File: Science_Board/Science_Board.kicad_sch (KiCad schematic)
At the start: 55 parts, among them J1 Conn_01x02, J10 Conn_01x02, J11 Conn_01x03, J12 Conn_01x03, J13 Conn_01x03, J14 Conn_01x03, J15 Conn_01x03, J16 Conn_01x03, J17 Conn_01x03, J18 Conn_01x03, J19 Conn_01x02, J2 RJ45_LED_Shielded, J20 Molex_Megafit_02, J22 Molex_Megafit_02, J23 Conn_01x02, J5 Conn_01x02, J6 Conn_01x04, J7 Conn_01x03, J8 Conn_01x03, J9 Conn_01x02, Q5 NMOS, SW1 SW_Push, SW10 SW_Push, SW11 SW_Push, SW12 SW_SPDT, SW2 SW_Push, SW3 SW_Push, SW4 SW_Push, SW5 SW_Push, SW6 SW_Push, SW7 SW_Push, SW8 SW_Push, SW9 SW_Push, U5 PCA9685BS

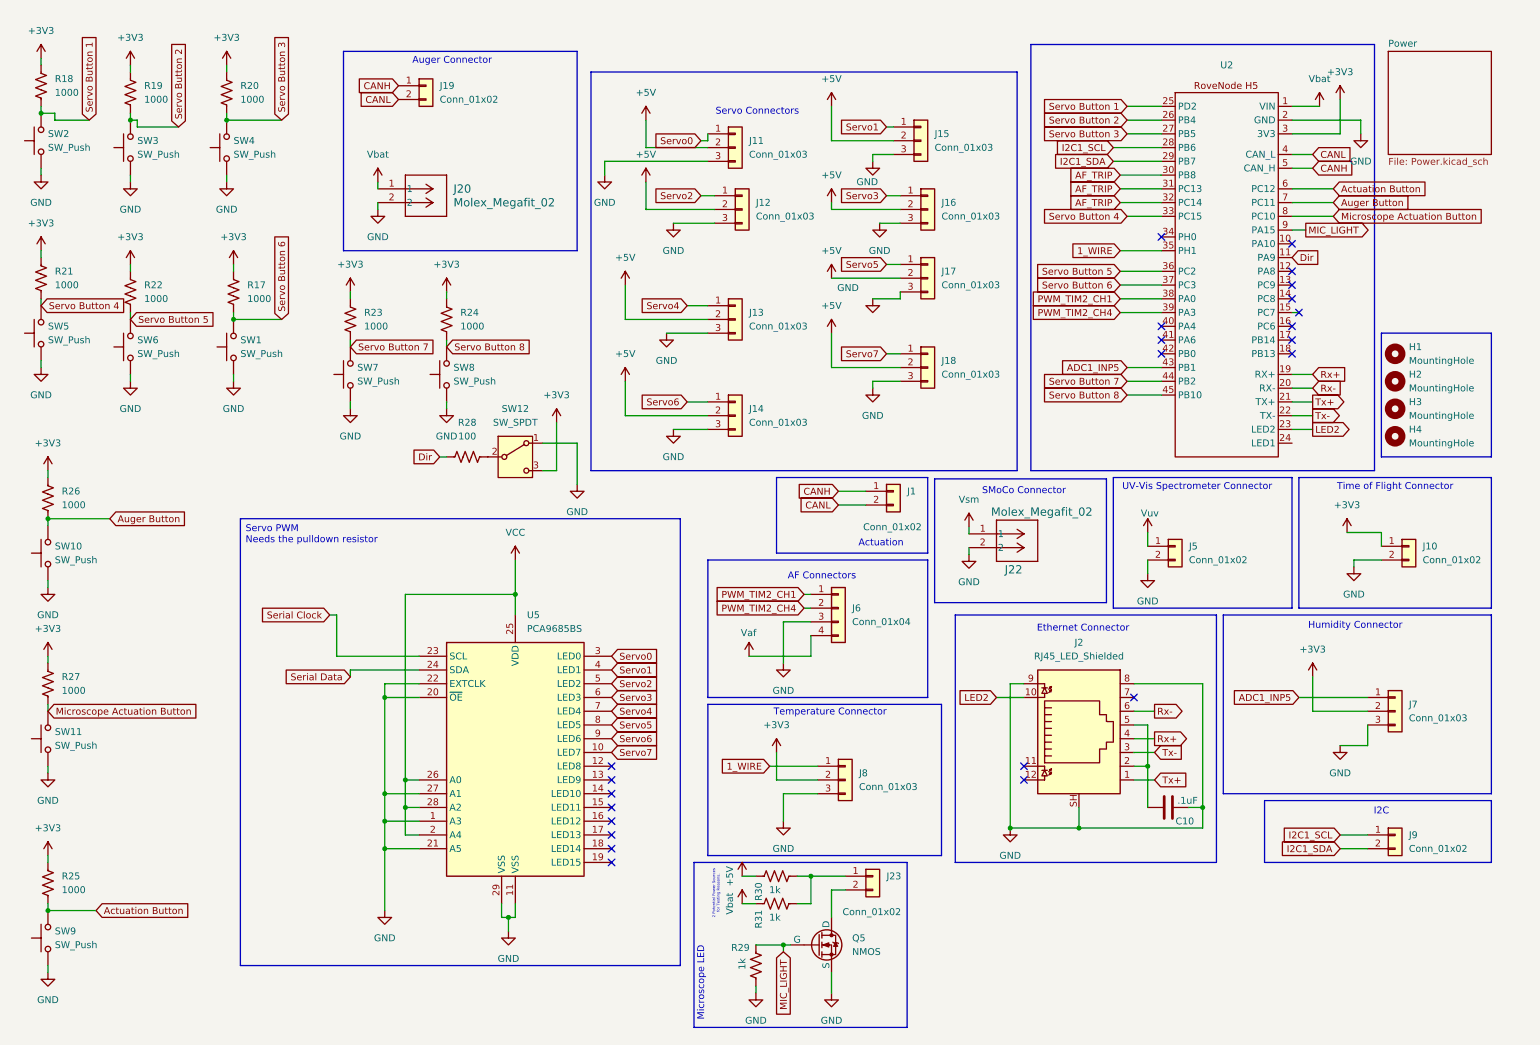
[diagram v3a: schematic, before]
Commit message: Incorrect Efuse Package, fixed and added gpio connections for loadswitch functionality
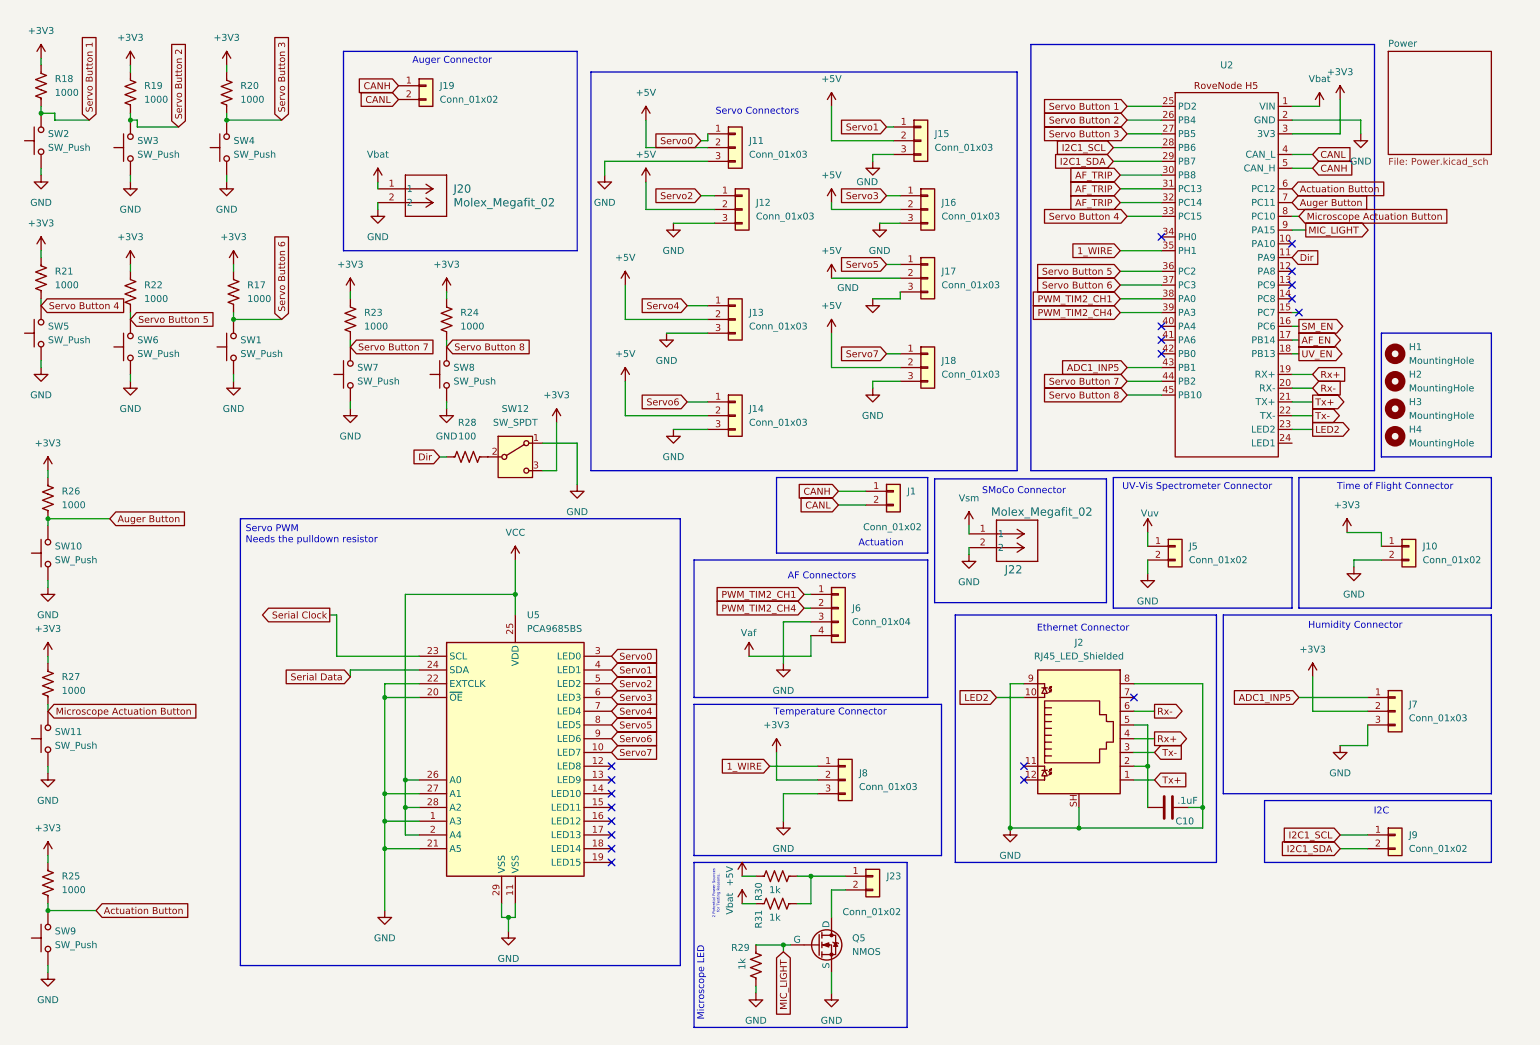
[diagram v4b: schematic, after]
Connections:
- net SM_EN: now reaches U2.16 (PC6)
- net AF_EN: now reaches U2.17 (PB14)
- net UV_EN: now reaches U2.18 (PB13)
- no-connect marks 23 -> 20
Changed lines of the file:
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@@
 	(paper "A4")
 	(rectangle
-		(start 138.43 135.89)
+		(start 135.89 135.89)
 		(end 181.61 163.83)
 		(stroke
@@
 	)
 	(rectangle
-		(start 138.43 109.22)
+		(start 135.89 109.22)
 		(end 179.07 134.62)
 		(stroke
@@
 	)
 	(no_connect
-		(at 246.38 71.12)
-	)
-	(no_connect
 		(at 120.65 162.56)
 	)
 	(no_connect
-		(at 246.38 66.04)
-	)
-	(no_connect
 		(at 246.38 55.88)
 	)
@@
 	)
 	(no_connect
-		(at 246.38 68.58)
-	)
-	(no_connect
 		(at 196.85 149.86)
 	)
@@
 	(wire
 		(pts
+			(xy 246.38 68.58) (xy 247.65 68.58)
+		)
+		(stroke
+			(width 0)
+			(type default)
+		)
+	)
+	(wire
+		(pts
 			(xy 152.4 180.34) (xy 153.67 180.34)
 		)
@@
 	(wire
 		(pts
-			(xy 246.38 43.18) (xy 254 43.18)
-		)
-		(stroke
-			(width 0)
-			(type default)
-		)
-	)
-	(wire
-		(pts
 			(xy 215.9 27.94) (xy 222.25 27.94)
 		)
@@
 	(wire
 		(pts
-			(xy 186.69 104.394) (xy 186.69 103.124)
-		)
-		(stroke
-			(width 0)
-			(type default)
-		)
-	)
-	(wire
-		(pts
 			(xy 171.45 29.21) (xy 172.72 29.21)
 		)
@@
 	(wire
 		(pts
+			(xy 186.69 102.87) (xy 186.69 104.394)
+		)
+		(stroke
+			(width 0)
+			(type default)
+		)
+	)
+	(wire
+		(pts
 			(xy 102.87 172.72) (xy 102.87 175.26)
 		)
@@
 	(wire
 		(pts
-			(xy 246.38 45.72) (xy 254 45.72)
+			(xy 246.38 45.72) (xy 247.65 45.72)
 		)
 		(stroke
@@
 	(wire
 		(pts
+			(xy 246.38 71.12) (xy 247.65 71.12)
+		)
+		(stroke
+			(width 0)
+			(type default)
+		)
+	)
+	(wire
+		(pts
 			(xy 215.9 45.72) (xy 222.25 45.72)
 		)
@@
 	(wire
 		(pts
-			(xy 246.38 40.64) (xy 254 40.64)
-		)
-		(stroke
-			(width 0)
-			(type default)
-		)
-	)
-	(wire
-		(pts
 			(xy 255.27 143.51) (xy 260.35 143.51)
 		)
@@
 	(wire
 		(pts
+			(xy 246.38 66.04) (xy 247.65 66.04)
+		)
+		(stroke
+			(width 0)
+			(type default)
+		)
+	)
+	(wire
+		(pts
 			(xy 171.45 71.12) (xy 173.99 71.12)
 		)
@@
 	)
 	(global_label "Serial Clock"
-		(shape input)
+		(shape output)
 		(at 68.58 119.38 180)
 		(fields_autoplaced yes)
@@
 	(global_label "Microscope Actuation Button"
 		(shape input)
-		(at 254 45.72 0)
+		(at 247.65 45.72 0)
 		(fields_autoplaced yes)
 		(effects
@@
 		)
 		(property "Intersheetrefs" "${INTERSHEET_REFS}"
-			(at 284.5015 45.72 0)
+			(at 278.1515 45.72 0)
 			(hide yes)
 			(show_name no)
@@
 		)
 	)
+	(global_label "UV_EN"
+		(shape output)
+		(at 247.65 71.12 0)
+		(fields_autoplaced yes)
+		(effects
+			(font
+				(size 1.27 1.27)
+				(thickness 0.1588)
+			)
+			(justify left)
+		)
+		(property "Intersheetrefs" "${INTERSHEET_REFS}"
+			(at 256.5014 71.12 0)
+			(hide yes)
+			(show_name no)
+			(do_not_autoplace no)
+			(effects
+				(font
+					(size 1.27 1.27)
+				)
+				(justify left)
+			)
+		)
+	)
 	(global_label "ADC1_INP5"
 		(shape input)
@@
 	(global_label "Actuation Button"
 		(shape input)
-		(at 254 40.64 0)
+		(at 246.38 40.64 0)
 		(fields_autoplaced yes)
 		(effects
@@
 		)
 		(property "Intersheetrefs" "${INTERSHEET_REFS}"
-			(at 272.9506 40.64 0)
+			(at 265.3306 40.64 0)
 			(hide yes)
 			(show_name no)
@@
 		)
 	)
+	(global_label "SM_EN"
+		(shape output)
+		(at 247.65 66.04 0)
+		(fields_autoplaced yes)
+		(effects
+			(font
+				(size 1.27 1.27)
+				(thickness 0.1588)
+			)
+			(justify left)
+		)
+		(property "Intersheetrefs" "${INTERSHEET_REFS}"
+			(at 256.7432 66.04 0)
+			(hide yes)
+			(show_name no)
+			(do_not_autoplace no)
+			(effects
+				(font
+					(size 1.27 1.27)
+				)
+				(justify left)
+			)
+		)
+	)
 	(global_label "MIC_LIGHT"
 		(shape output)
@@
 		)
 	)
+	(global_label "AF_EN"
+		(shape output)
+		(at 247.65 68.58 0)
+		(fields_autoplaced yes)
+		(effects
+			(font
+				(size 1.27 1.27)
+				(thickness 0.1588)
+			)
+			(justify left)
+		)
+		(property "Intersheetrefs" "${INTERSHEET_REFS}"
+			(at 256.2595 68.58 0)
+			(hide yes)
+			(show_name no)
+			(do_not_autoplace no)
+			(effects
+				(font
+					(size 1.27 1.27)
+				)
+				(justify left)
+			)
+		)
+	)
 	(global_label "Servo Button 1"
 		(shape input)
@@
 	(global_label "Auger Button"
 		(shape input)
-		(at 254 43.18 0)
+		(at 246.38 43.18 0)
 		(fields_autoplaced yes)
 		(effects
@@
 		)
 		(property "Intersheetrefs" "${INTERSHEET_REFS}"
-			(at 269.3826 43.18 0)
+			(at 261.7626 43.18 0)
 			(hide yes)
 			(show_name no)
@@
 	(symbol
 		(lib_id "power:VCC")
-		(at 186.69 103.124 0)
+		(at 186.69 102.87 0)
 		(unit 1)
 		(body_style 1)
@@
 		(fields_autoplaced yes)
 		(property "Reference" "#PWR093"
-			(at 186.69 106.934 0)
+			(at 186.69 106.68 0)
 			(hide yes)
 			(show_name no)
@@
 		)
 		(property "Value" "Vsm"
-			(at 186.69 98.044 0)
+			(at 186.69 97.79 0)
 			(show_name no)
 			(do_not_autoplace no)
@@
 		)
 		(property "Footprint" "MRDT_Connectors:MOLEX_MegaFit_02_Horizontal"
-			(at 186.69 103.124 0)
+			(at 186.69 102.87 0)
 			(hide yes)
 			(show_name no)
@@
 		)
 		(property "Datasheet" ""
-			(at 186.69 103.124 0)
+			(at 186.69 102.87 0)
 			(hide yes)
 			(show_name no)
@@
 		)
 		(property "Description" "Power symbol creates a global label with name \"VCC\""
-			(at 186.69 103.124 0)
+			(at 186.69 102.87 0)
 			(hide yes)
 			(show_name no)

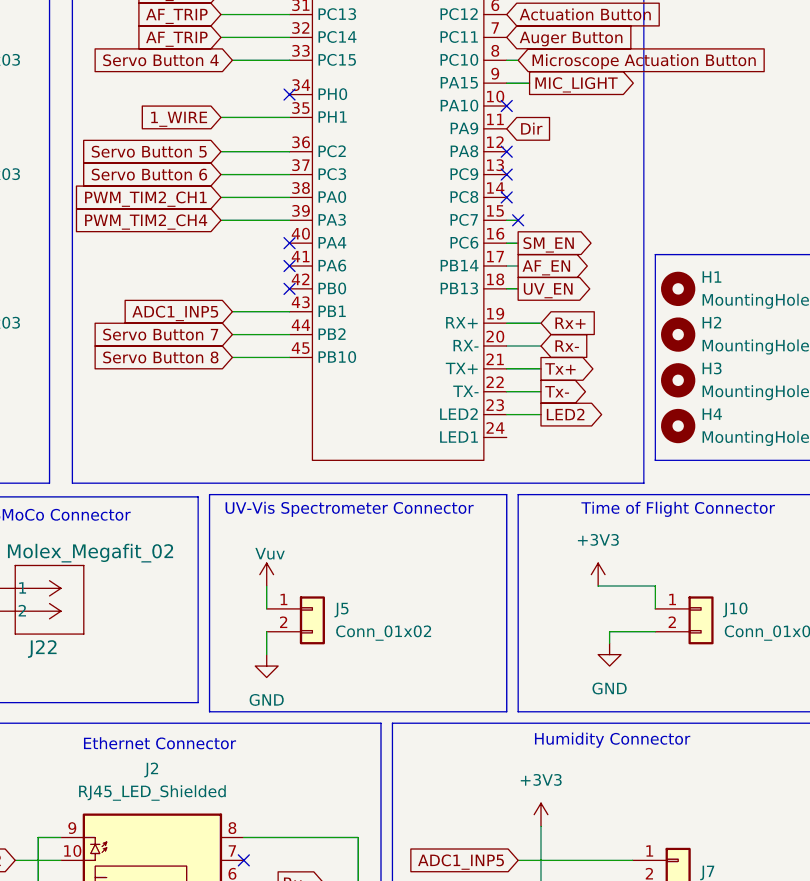
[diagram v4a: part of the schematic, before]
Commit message: added mode selectors for UV-Vis
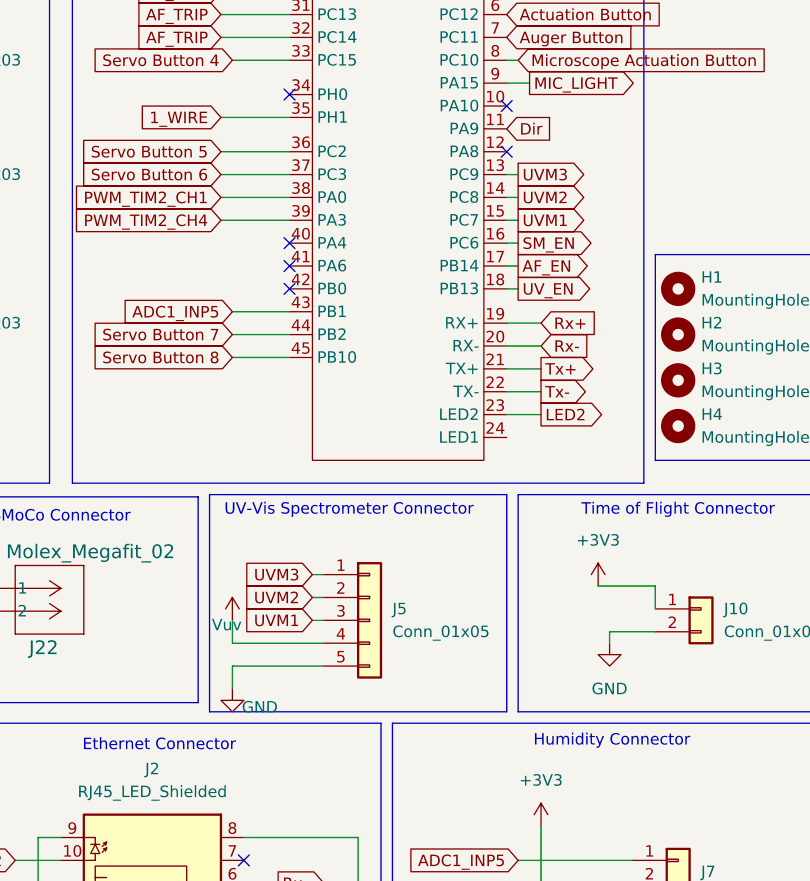
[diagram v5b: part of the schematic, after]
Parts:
- removed J5: Conn_01x02, Connector_JST:JST_PH_B2B-PH-K_1x02_P2.00mm_Vertical, symbol Connector_Generic:Conn_01x02
- added J5: Conn_01x05, Package_DFN_QFN:QFN-20-1EP_5x5mm_P0.65mm_EP3.35x3.35mm, symbol Connector_Generic:Conn_01x05
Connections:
- net GND: now also J5.5 (Pin_5)
- net Vuv: now also J5.4 (Pin_4)
- net UVM3: now reaches U2.13 (PC9)
- net UVM3: now also J5.1 (Pin_1)
- net UVM2: now reaches U2.14 (PC8)
- net UVM2: now also J5.2 (Pin_2)
- net UVM1: now reaches U2.15 (PC7)
- net UVM1: now also J5.3 (Pin_3)
- no-connect marks 20 -> 17
